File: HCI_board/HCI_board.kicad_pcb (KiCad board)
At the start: 2 copper layers, 29.9 x 83.1 mm, 32 parts, among them J1 MCU Controls, J3 Power, J4 USB Data, J7 DC Motor Terminal, J9 USBC_RECP, SW1 Trigger, SW2 Increment, SW3 Reset, SW4 Decrement, U1 NCP1117, U2 ICM7555xB, U3 DRV8833PWP

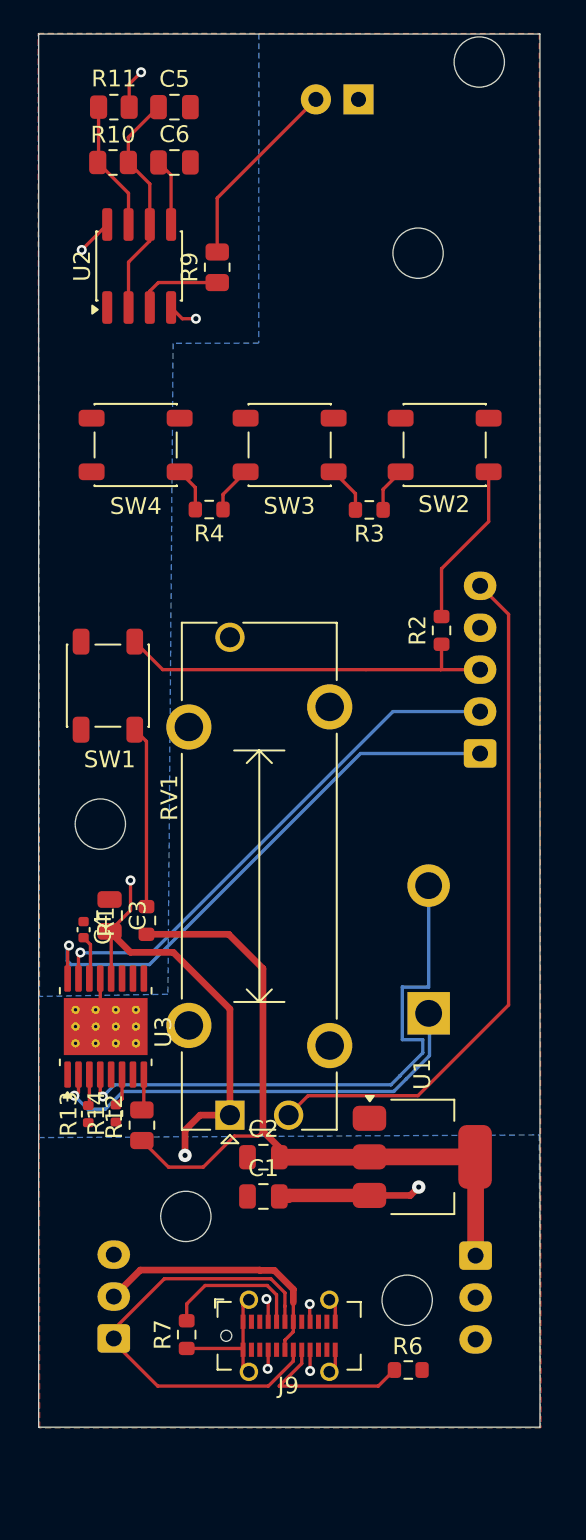
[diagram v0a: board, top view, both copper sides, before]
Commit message: Updated PCB from schematic changes
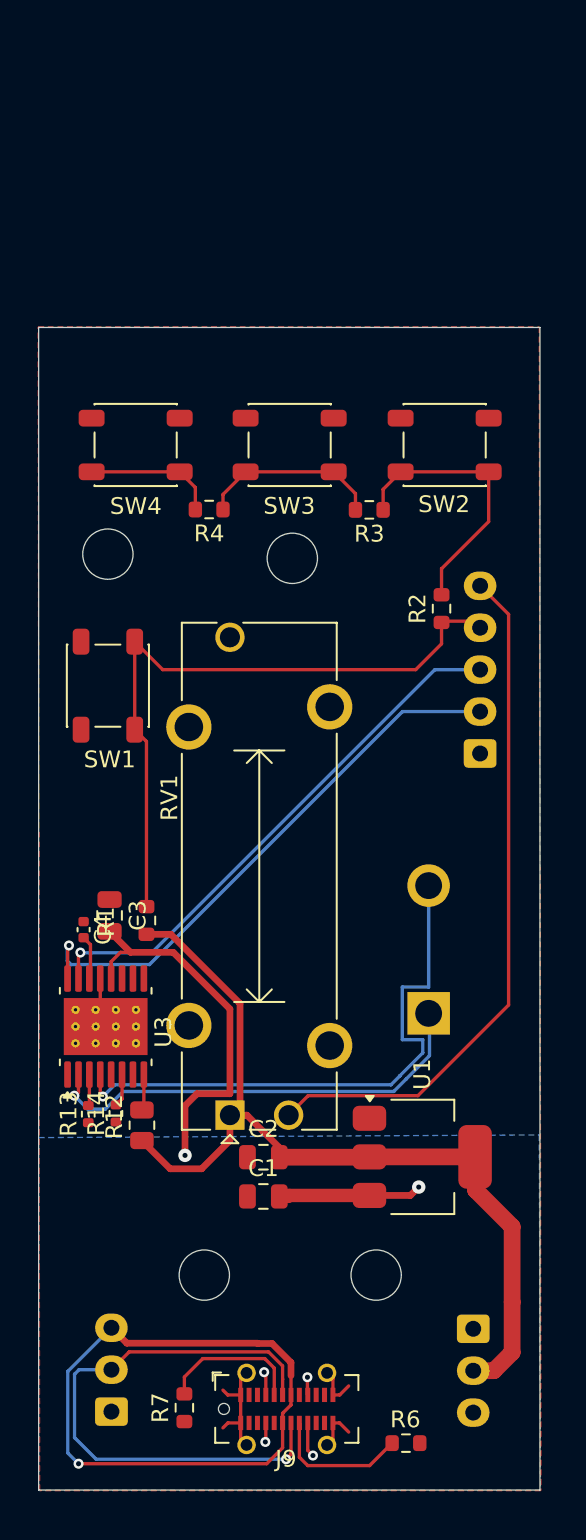
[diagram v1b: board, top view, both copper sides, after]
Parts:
- removed C5: 1n, Capacitor_SMD:C_0805_2012Metric
- removed C6: 10n, Capacitor_SMD:C_0805_2012Metric
- removed D1: IR204A, LED_THT:LED_D3.0mm_IRBlack
- removed R10: 20k, Resistor_SMD:R_0805_2012Metric
- removed R11: 1k, Resistor_SMD:R_0805_2012Metric
- removed R9: 22, Resistor_SMD:R_0805_2012Metric
- removed U2: ICM7555xB, Package_SO:SOIC-8_3.9x4.9mm_P1.27mm
- moved R6 4.36 mm to (141.8, 145.0)
- moved J3 4.36 mm to (145.8, 138.2)
- moved J4 4.36 mm to (124.2, 143.1)
- moved J9 4.36 mm to (134.7, 143.0)
- moved R7 4.36 mm to (128.6, 142.9)
- moved R2 1.30 mm to (143.9, 95.2)
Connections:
- J1 pad 1: /AIN1 -> GND
- J1 pad 2: /AIN2 -> /AIN1
- J1 pad 3: /BTN -> /AIN2
- J1 pad 4: GND -> /BTN
- J3 pad 1: +3.3V -> GND
- J3 pad 2: GND -> +3.3V
- J4 pad 1: /USB D+ -> GND
- J4 pad 2: /USB D- -> /USB D+
- J4 pad 3: GND -> /USB D-
- RV1 pad 1: +5V -> +3.3V
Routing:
- net /USB D-: track 15.7 -> 38.9 mm, vias 0 -> 1
- net Net-(U2-THR): track 13.8 -> 0.00 mm
- net Net-(D1-A): track 11.5 -> 0.00 mm
- net +5V: track 45.9 -> 36.6 mm, vias 10 -> 6
- net +3.3V: track 45.6 -> 53.5 mm
- net Net-(U2-DIS): track 7.78 -> 0.00 mm
- net /USB D+: track 27.4 -> 34.3 mm, vias 0 -> 1
- net /BTN: track 33.7 -> 39.5 mm
- net Net-(R3-Pad2): track 5.62 -> 10.9 mm
- net Net-(R4-Pad2): track 2.64 -> 7.89 mm
- net Net-(U2-Q): track 5.21 -> 0.00 mm
- net Net-(U2-CV): track 4.01 -> 0.00 mm
- net Net-(R2-Pad2): track 13.3 -> 17.2 mm
- net GND: track 14.5 -> 16.6 mm
- net Net-(J9-CC2): track 9.99 -> 8.34 mm
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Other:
- board size 29.9 x 83.1 mm -> 29.9 x 69.3 mm

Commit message: fixed rule errors
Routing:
- net +3.3V: track 53.5 -> 54.4 mm
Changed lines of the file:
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@@
 		(tags "capacitor")
 		(property "Reference" "C2"
-			(at 0 -1.68 0)
+			(at -2.775 0.03 0)
 			(layer "F.SilkS")
 			(effects
@@
 		(tags "resistor")
 		(property "Reference" "R13"
-			(at 0 -1.17 90)
+			(at -2.5 -0.23 90)
 			(layer "F.SilkS")
 			(effects
@@
 		(tags "HTSSOP SO Texas_PWP0016C Texas_PowerPAD-TSSOP")
 		(property "Reference" "U3"
-			(at -0.3225 3.44 90)
+			(at -3.3225 -3.27 270)
 			(layer "F.SilkS")
 			(effects
@@
 		(tags "capacitor")
 		(property "Reference" "C4"
-			(at 0 -1.16 90)
+			(at -1.6975 0.65 180)
 			(layer "F.SilkS")
 			(effects
@@
 		(tags "capacitor")
 		(property "Reference" "C1"
-			(at 0 -1.68 0)
+			(at -2.775 0.09 0)
 			(layer "F.SilkS")
 			(effects
@@
 		)
 		(property "Value" "10u"
-			(at -0.13924 6.04224 0)
+			(at 0.125 1.89 0)
 			(layer "F.Fab")
 			(effects
@@
 		(tags "CMS SOT")
 		(property "Reference" "U1"
-			(at 0 -4.93 90)
+			(at -0.05 4.65 180)
 			(layer "F.SilkS")
 			(effects
@@
 		(tags "resistor")
 		(property "Reference" "R12"
-			(at 0.5125 -1.65 90)
+			(at -3.1375 0.07 90)
 			(layer "F.SilkS")
 			(effects
@@
 		(tags "resistor")
 		(property "Reference" "R14"
-			(at 0 -1.17 90)
+			(at -2.54 -0.28 90)
 			(layer "F.SilkS")
 			(effects
@@
 		(tags "capacitor")
 		(property "Reference" "C3"
-			(at 0 -1.68 90)
+			(at -2.65 -0.1 180)
 			(layer "F.SilkS")
 			(effects
@@
 		(tags "USB C Type-C Receptacle SMD")
 		(property "Reference" "J9"
-			(at -0.05 2.98 0)
+			(at -4.27076 3.01776 0)
 			(layer "F.SilkS")
 			(effects
@@
 		(tags "resistor")
 		(property "Reference" "R1"
-			(at -0.0775 -2.41 90)
+			(at 2.35 0.1 180)
 			(layer "F.SilkS")
 			(effects
@@
 		(tags "connector JST EH vertical")
 		(property "Reference" "J1"
-			(at 5 2.8 270)
+			(at -2.21 -3.6 270)
 			(layer "B.SilkS")
 			(effects
@@
 	)
 	(segment
-		(start 131.28 125.46)
-		(end 131.28 126.97)
+		(start 129.6 128.3)
+		(end 129.239 128.661)
 		(width 0.4)
 		(layer "F.Cu")
@@
 	)
 	(segment
-		(start 131.28 126.97)
-		(end 129.589 128.661)
+		(start 145.79076 140.70224)
+		(end 147.02076 140.70224)
+		(width 1)
+		(layer "F.Cu")
+		(net 3)
+	)
+	(segment
+		(start 134.225 127.97)
+		(end 134.225 126.76)
 		(width 0.4)
 		(layer "F.Cu")
@@
 	)
 	(segment
-		(start 145.79076 140.70224)
-		(end 147.02076 140.70224)
-		(width 1)
+		(start 131.28 125.46)
+		(end 130.04 125.46)
+		(width 0.4)
+		(layer "F.Cu")
+		(net 3)
+	)
+	(segment
+		(start 130.04 125.46)
+		(end 129.6 125.9)
+		(width 0.4)
 		(layer "F.Cu")
 		(net 3)
@@
 	)
 	(segment
-		(start 131.28 125.46)
-		(end 131.881 124.859)
+		(start 132.925 125.46)
+		(end 131.28 125.46)
 		(width 0.4)
 		(layer "F.Cu")
@@
 	)
 	(segment
-		(start 132.29 125.46)
-		(end 133.25 126.42)
+		(start 131.28 125.46)
+		(end 131.881 124.859)
 		(width 0.4)
 		(layer "F.Cu")
@@
 	)
 	(segment
-		(start 134.225 127.97)
-		(end 134.225 127.395)
-		(width 0.4)
-		(layer "F.Cu")
-		(net 3)
-	)
-	(segment
 		(start 148.11076 139.61224)
 		(end 148.11076 136.61224)
@@
 	)
 	(segment
-		(start 129.589 128.661)
-		(end 127.716 128.661)
+		(start 134.225 126.76)
+		(end 132.925 125.46)
 		(width 0.4)
 		(layer "F.Cu")
@@
 	)
 	(segment
+		(start 129.6 125.9)
+		(end 129.6 128.3)
+		(width 0.4)
+		(layer "F.Cu")
+		(net 3)
+	)
+	(segment
 		(start 139.58 127.97)
 		(end 139.6 127.95)
@@
 	)
 	(segment
+		(start 127.716 128.661)
+		(end 126.03 126.975)
+		(width 0.4)
+		(layer "F.Cu")
+		(net 3)
+	)
+	(segment
 		(start 145.9 127.95)
 		(end 139.6 127.95)
@@
 	)
 	(segment
-		(start 134.225 127.395)
-		(end 133.25 126.42)
-		(width 0.4)
-		(layer "F.Cu")
-		(net 3)
-	)
-	(segment
-		(start 131.28 125.46)
-		(end 132.29 125.46)
-		(width 0.4)
-		(layer "F.Cu")
-		(net 3)
-	)
-	(segment
-		(start 127.716 128.661)
-		(end 126.03 126.975)
+		(start 129.239 128.661)
+		(end 127.716 128.661)
 		(width 0.4)
 		(layer "F.Cu")
@@
 		(polygon
 			(pts
-				(xy 119.9 147.85) (xy 119.87 126.8) (xy 149.73 126.64) (xy 149.8 147.85)
+				(xy 119.7 148) (xy 119.693311 78.279875) (xy 149.9 78.3) (xy 150 148)
 			)
 		)

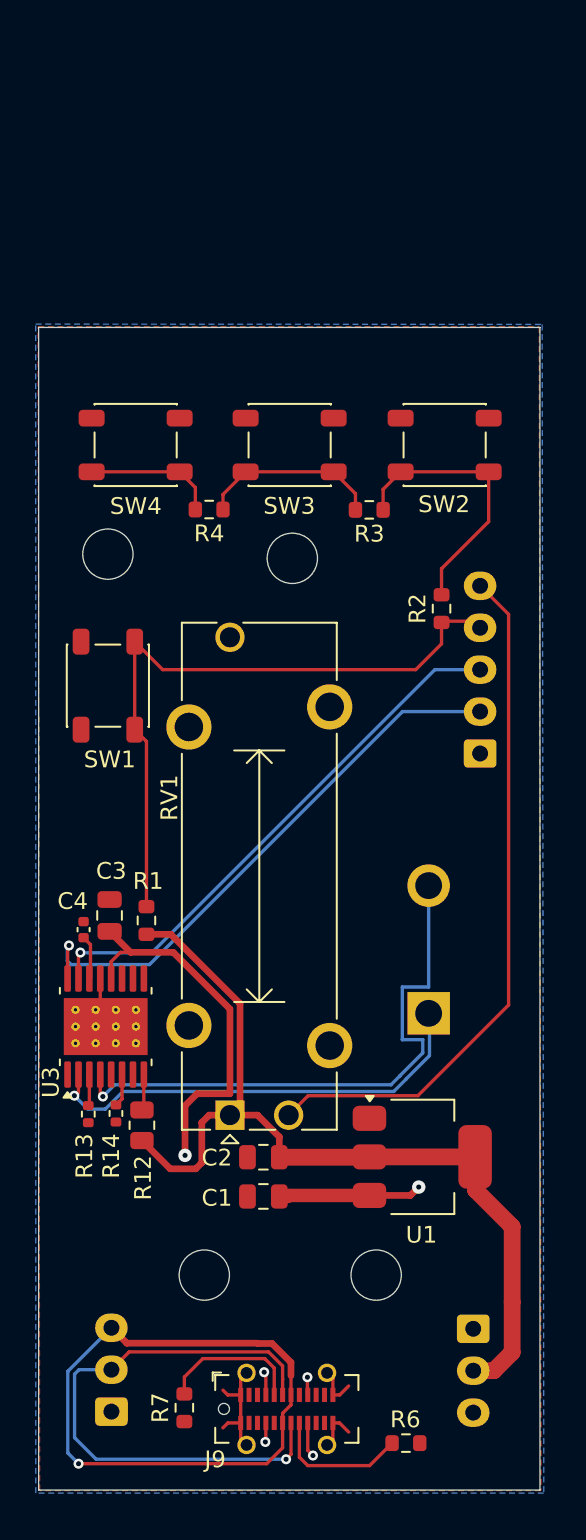
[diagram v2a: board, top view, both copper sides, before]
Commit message: updated mounting holes
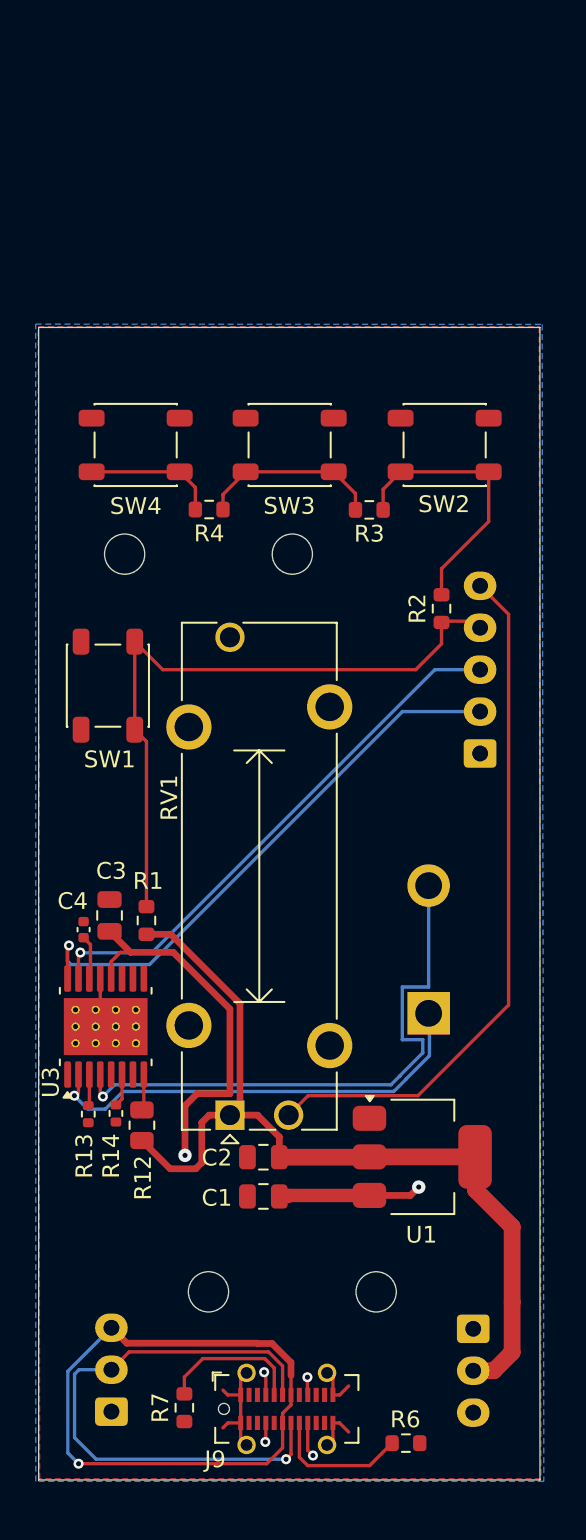
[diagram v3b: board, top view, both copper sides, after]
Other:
- board size 29.9 x 69.3 mm -> 29.9 x 68.7 mm
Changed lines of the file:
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@@
 		)
 	)
+	(property "SCREW_HOLE_DIAM" "1.2")
 	(net 0 "")
 	(net 1 "GND")
@@
 			(at -1 -1.8 90)
 			(size 0.5 0.5)
-			(drill 0.2)
+			(drill 0.3)
 			(property pad_prop_heatsink)
 			(layers "*.Cu")
@@
 			(at -1 -0.6 90)
 			(size 0.5 0.5)
-			(drill 0.2)
+			(drill 0.3)
 			(property pad_prop_heatsink)
 			(layers "*.Cu")
@@
 			(at -1 0.6 90)
 			(size 0.5 0.5)
-			(drill 0.2)
+			(drill 0.3)
 			(property pad_prop_heatsink)
 			(layers "*.Cu")
@@
 			(at -1 1.8 90)
 			(size 0.5 0.5)
-			(drill 0.2)
+			(drill 0.3)
 			(property pad_prop_heatsink)
 			(layers "*.Cu")
@@
 			(at 0 -1.8 90)
 			(size 0.5 0.5)
-			(drill 0.2)
+			(drill 0.3)
 			(property pad_prop_heatsink)
 			(layers "*.Cu")
@@
 			(at 0 -0.6 90)
 			(size 0.5 0.5)
-			(drill 0.2)
+			(drill 0.3)
 			(property pad_prop_heatsink)
 			(layers "*.Cu")
@@
 			(at 0 0.6 90)
 			(size 0.5 0.5)
-			(drill 0.2)
+			(drill 0.3)
 			(property pad_prop_heatsink)
 			(layers "*.Cu")
@@
 			(at 0 1.8 90)
 			(size 0.5 0.5)
-			(drill 0.2)
+			(drill 0.3)
 			(property pad_prop_heatsink)
 			(layers "*.Cu")
@@
 			(at 1 -1.8 90)
 			(size 0.5 0.5)
-			(drill 0.2)
+			(drill 0.3)
 			(property pad_prop_heatsink)
 			(layers "*.Cu")
@@
 			(at 1 -0.6 90)
 			(size 0.5 0.5)
-			(drill 0.2)
+			(drill 0.3)
 			(property pad_prop_heatsink)
 			(layers "*.Cu")
@@
 			(at 1 0.6 90)
 			(size 0.5 0.5)
-			(drill 0.2)
+			(drill 0.3)
 			(property pad_prop_heatsink)
 			(layers "*.Cu")
@@
 			(at 1 1.8 90)
 			(size 0.5 0.5)
-			(drill 0.2)
+			(drill 0.3)
 			(property pad_prop_heatsink)
 			(layers "*.Cu")
@@
 	)
 	(gr_circle
-		(center 140 135)
-		(end 141.5 135)
+		(center 140 136)
+		(end 141.2 136)
 		(stroke
 			(width 0.05)
@@
 	)
 	(gr_circle
-		(center 135 92.25)
-		(end 136.5 92.25)
+		(center 135 92)
+		(end 136.2 92)
 		(stroke
 			(width 0.05)
@@
 	(gr_rect
 		(start 119.87 78.48)
-		(end 149.77 147.82)
+		(end 149.77 147.22)
 		(stroke
 			(width 0.05)
@@
 	)
 	(gr_circle
-		(center 124 92)
-		(end 125.5 92)
+		(center 125 92)
+		(end 126.2 92)
 		(stroke
 			(width 0.05)
@@
 	)
 	(gr_circle
-		(center 129.75 135)
-		(end 131.25 135)
+		(center 130 136)
+		(end 131.2 136)
 		(stroke
 			(width 0.05)
@@
 		(layer "Edge.Cuts")
 	)
+	(gr_circle
+		(center 130 136)
+		(end 132.25 136)
+		(stroke
+			(width 0.1)
+			(type dash)
+		)
+		(fill no)
+		(layer "User.1")
+	)
+	(gr_circle
+		(center 140 136)
+		(end 142.25 136)
+		(stroke
+			(width 0.1)
+			(type dash)
+		)
+		(fill no)
+		(layer "User.1")
+	)
+	(gr_line
+		(start 125 92)
+		(end 135 92)
+		(stroke
+			(width 0.1)
+			(type solid)
+		)
+		(layer "User.1")
+	)
+	(gr_circle
+		(center 125 92)
+		(end 127.25 92)
+		(stroke
+			(width 0.1)
+			(type dash)
+		)
+		(fill no)
+		(layer "User.1")
+	)
+	(gr_line
+		(start 130 136)
+		(end 140 136)
+		(stroke
+			(width 0.1)
+			(type solid)
+		)
+		(layer "User.1")
+	)
+	(gr_circle
+		(center 135 92)
+		(end 137.25 92)
+		(stroke
+			(width 0.1)
+			(type dash)
+		)
+		(fill no)
+		(layer "User.1")
+	)
 	(segment
 		(start 132.03076 140.59224)
@@
 		(net 1)
 		(net_name "GND")
-		(locked yes)
 		(layer "F.Cu")
 		(hatch edge 0.5)
@@
 		(polygon
 			(pts
-				(xy 119.84 78.45) (xy 149.73 78.45) (xy 149.83 147.85) (xy 119.93 147.85)
+				(xy 119.84 78.45) (xy 149.73 78.45) (xy 149.83 147.15) (xy 119.93 147.15)
 			)
 		)
@@
 		(net 2)
 		(net_name "+5V")
-		(locked yes)
 		(layer "B.Cu")
 		(hatch edge 0.5)
@@
 		(polygon
 			(pts
-				(xy 119.7 148) (xy 119.693311 78.279875) (xy 149.9 78.3) (xy 150 148)
+				(xy 119.7 147.3) (xy 119.693311 78.279875) (xy 149.9 78.3) (xy 150 147.3)
 			)
 		)
 	)
+	(group ""
+		(members "062beeab-17a6-4253-bc82-3d13b5ea3ff7" "c64a80fc-ed3b-40bf-93e0-c05419d61be0"
+			"f1ac13bb-0c0a-49e1-a7ee-41aa009df262"
+		)
+	)

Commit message: updated mount holes AGAIN! Slightly resized boards and made mount holes better
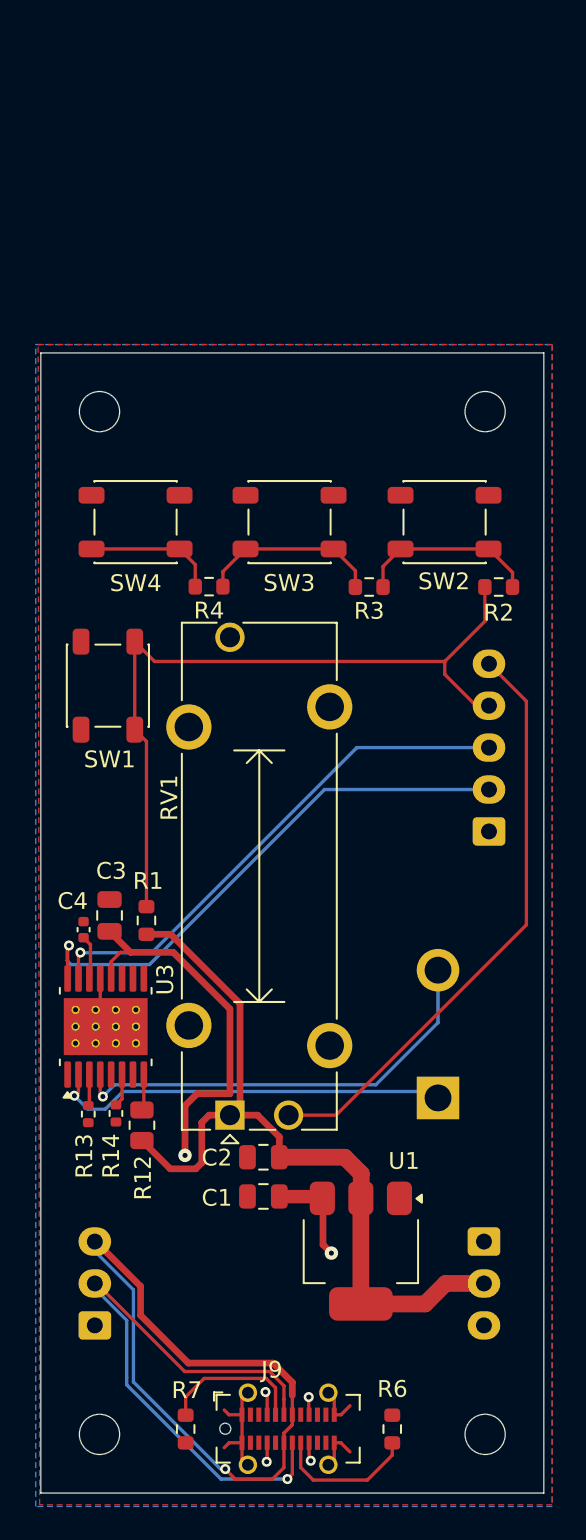
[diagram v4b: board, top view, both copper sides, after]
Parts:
- moved U1 6.71 mm to (139.1, 133.6), turned to -90 degrees
- moved J3 5.24 mm to (146.4, 133.0)
- moved J4 5.24 mm to (123.2, 138.0)
- moved J7 5.08 mm to (143.7, 124.4)
- moved J1 4.68 mm to (146.7, 108.5)
- moved SW2 4.60 mm to (144.1, 90.1)
- moved SW3 4.60 mm to (134.8, 90.1)
- moved SW4 4.60 mm to (125.7, 90.1)
- moved R3 4.60 mm to (139.6, 94.0)
- moved R4 4.60 mm to (130.0, 93.9)
- moved R2 3.65 mm to (147.3, 94.0), turned to 0 degrees
- moved R7 1.27 mm to (128.6, 144.2)
- moved J9 1.19 mm to (134.8, 144.2)
- moved R6 1.17 mm to (141.0, 144.2), turned to -90 degrees
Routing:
- net Net-(J7-Pin_2): track 34.3 -> 26.3 mm
- net /POT: track 41.5 -> 35.4 mm
- net Net-(R2-Pad2): track 17.2 -> 11.1 mm
- net +3.3V: track 54.4 -> 48.8 mm
- net /BTN: track 39.5 -> 44.7 mm
- net /USB D-: track 38.9 -> 42.7 mm
- net +5V: track 36.6 -> 33.7 mm
- net Net-(J7-Pin_1): track 26.8 -> 24.1 mm
- net /USB D+: track 34.3 -> 36.7 mm
- net /AIN1: track 34.2 -> 32.8 mm
- net /AIN2: track 32.4 -> 31.0 mm
- net GND: track 16.6 -> 15.8 mm
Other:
- board size 29.9 x 68.7 mm -> 30 x 68 mm

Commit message: added test points
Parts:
- added TP1: GND, TestPoint:TestPoint_Pad_2.0x2.0mm, F.Cu at (127.2, 132.8)
- added TP2: 5V, TestPoint:TestPoint_Pad_D2.0mm, F.Cu at (133.6, 133.7)
- added TP3: 3V3, TestPoint:TestPoint_Pad_D2.0mm, F.Cu at (133.5, 136.8)
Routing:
- net +3.3V: track 48.8 -> 54.5 mm
- net +5V: track 33.7 -> 37.4 mm
